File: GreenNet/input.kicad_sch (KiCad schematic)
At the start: 27 parts, among them U2 USB_C_Receptacle_12P, U3 USB_C_Receptacle_12P, U4 CP2102N-A02-GQFN28

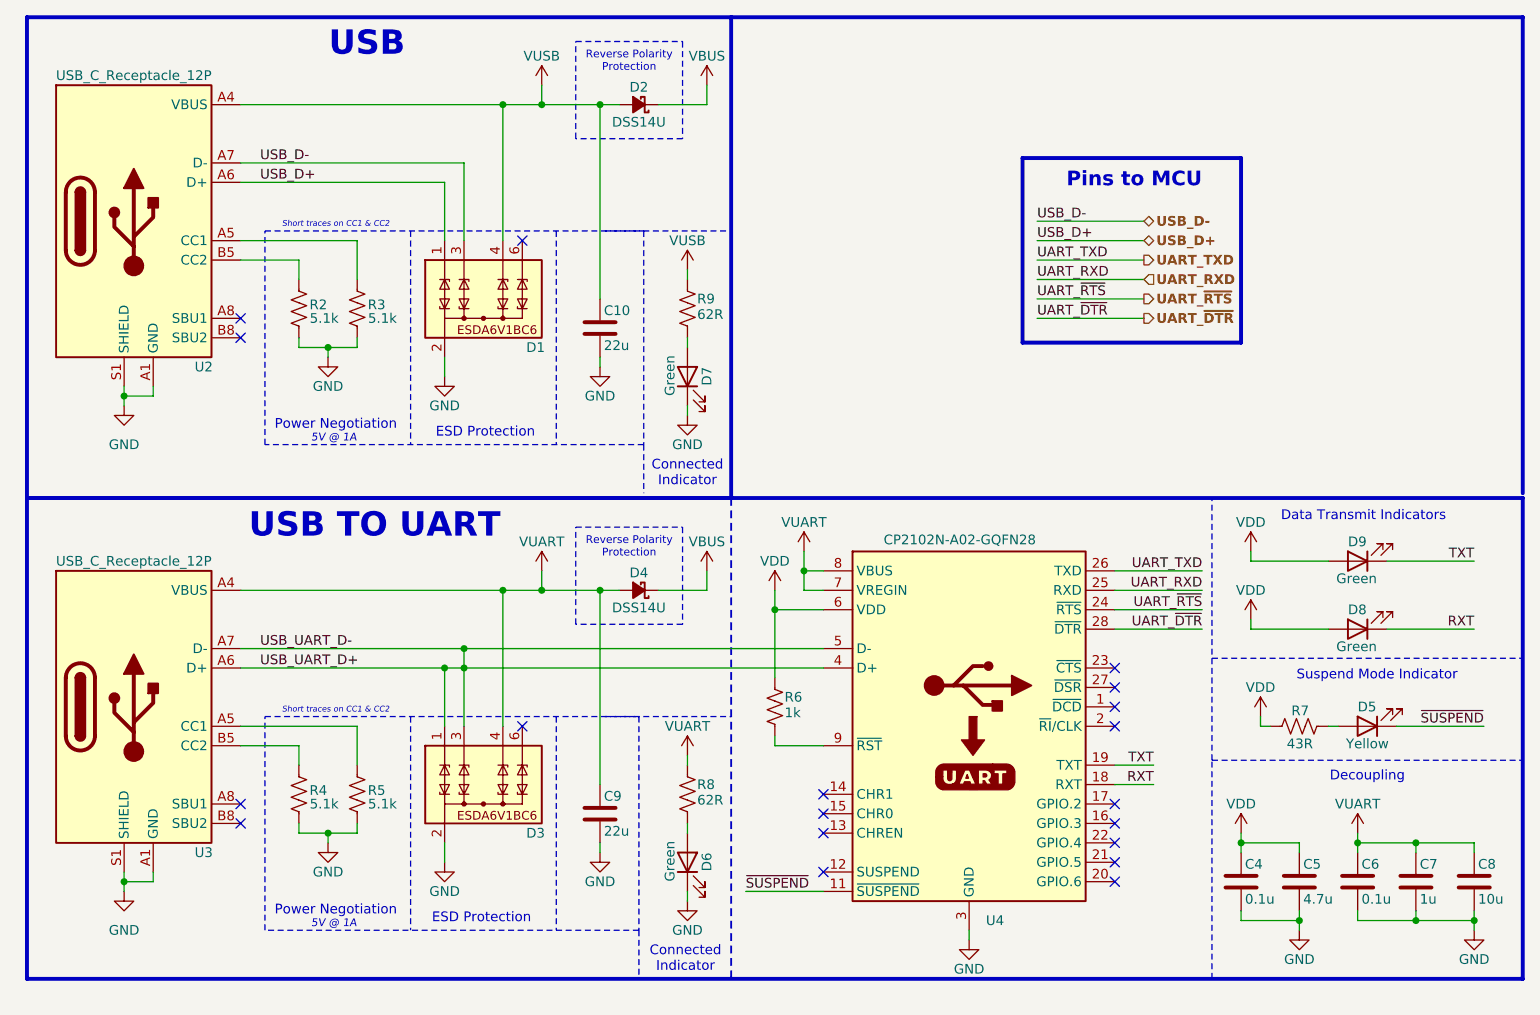
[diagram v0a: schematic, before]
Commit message: finished input schematic
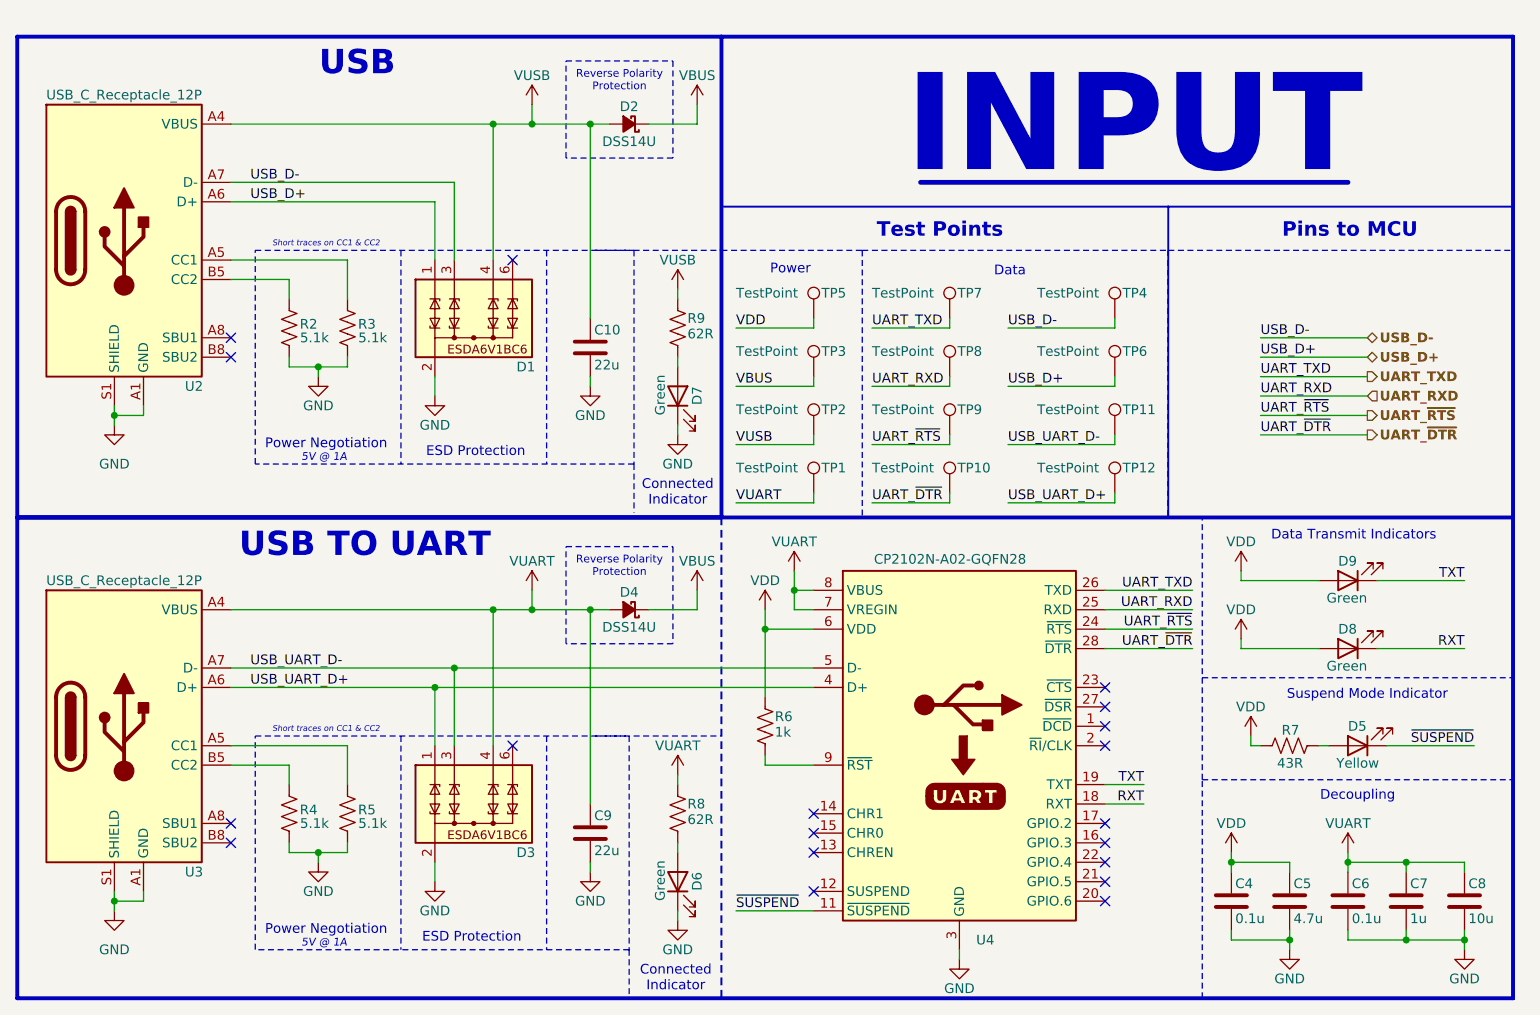
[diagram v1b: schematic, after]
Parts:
- added TP1, TP10, TP11, TP12, TP2, TP3, TP4, TP5, TP6, TP7, TP8, TP9: TestPoint, AA_TestPoints:RCWCTE, symbol Connector:TestPoint
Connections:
- net UART_RXD: now also TP8.1
- net UART_TXD: now also TP7.1
- net UART_~{DTR}: now also TP10.1
- net UART_~{RTS}: now also TP9.1
- net USB_D+: now also TP6.1
- net USB_D-: now also TP4.1
- net USB_UART_D+: now also TP12.1; no longer D3.3 (TVS2), U3.A7 (D-), U3.B7 (D-), U4.5 (D-)
- net VBUS: now also TP3.1
- net VDD: now also TP5.1
- net VUART: now also TP1.1
- net VUSB: now also TP2.1
- new net USB_UART_D-: D3.3 (TVS2), TP11.1, U3.A7 (D-), U3.B7 (D-), U4.5 (D-)
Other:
- note added: "Data"
- note added: "INPUT"
- note added: "Power"
- note added: "Test Points"
- moved on the sheet: C10, C4, C5, C6, C7, C8, C9, D1, D2, D3, D4, D5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

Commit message: USB-PC PD progress
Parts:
- removed R2, R3: 5.1k, Resistor_SMD:R_0805_2012Metric, symbol Device:R_US
- removed TP1, TP10, TP11, TP12, TP2, TP3, TP4, TP5, TP6, TP7, TP8, TP9: TestPoint, AA_TestPoints:RCWCTE, symbol Connector:TestPoint
- added Q4: IRF9358TRPBF, AA_FETS:SO8_IRF9358TRPBF_INF, symbol AA_FETs:IRF9358TRPBF
- added TP13, TP14, TP15, TP16, TP17, TP18, TP19, TP20, TP21, TP22, TP23, TP24: TestPoint, AA_TestPoints:RCWCTE, symbol Connector:TestPoint
- added U6: CYPD3177-24LQXQT, AA_Interface_USB:QFN50P400X400X60-25N-D, symbol AA_Interface_USB:CYPD3177-24LQXQT
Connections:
- net UART_RXD: now also TP18.1
- net UART_TXD: now also TP17.1
- net UART_~{DTR}: now also TP20.1
- net UART_~{RTS}: now also TP19.1
- net USB_D+: now also TP22.1
- net USB_D-: now also TP21.1
- net USB_UART_D+: now also TP24.1
- net USB_UART_D-: now also TP23.1
- net VBUS: now also TP14.1
- net VDD: no longer R6.1, U4.6 (VDD)
- net VUART: now also TP16.1
- net VUSB: now also TP15.1, U6.18 (VBUS_IN)
- net USB_CC1: now reaches U2.A5 (CC1)
- net USB_CC1: now also U6.15 (CC1)
- net USB_CC2: now reaches U2.B5 (CC2)
- net USB_CC2: now also U6.14 (CC2)
- net GND renamed EP
- net EP: now also U6.19 (GND), U6.22 (GND), U6.25 (EP)
- new net: U6.20 (DNU), U6.21 (DNU)
- new net: Q4.1 (S2), Q4.3 (S1)
- new net: Q4.5 (D1), Q4.6 (D1)
- new net ISINK_FINE: U6.6 (ISNK_FINE)
- new net ISNK_COARSE: U6.5 (ISNK_COARSE)
- new net SAFE_PWR_EN: U6.4 (SAFE_PWR_EN)
- new net UART_VDD: R6.1, TP13.1, U4.6 (VDD)
- new net USB_FAULT: U6.9 (FAULT)
- new net USB_FLIP: U6.10 (FLIP)
- new net USB_GPIO: U6.8 (GPIO)
- new net USB_HPI_INT: U6.7 (HPI_INT)
- new net USB_HPI_SCL: U6.13 (HPI_SCL)
- new net USB_HPI_SDA: U6.12 (HPI_SDA)
- new net USB_VCC: U6.24 (VCCD)
- new net USB_VDC_OUT: Q4.7 (D2), Q4.8 (D2), U6.11 (VDC_OUT)
- new net USB_VDD: U6.23 (VDDD)
- new net VBUS_FET_EN: U6.3 (VBUS_FET_EN)
- new net VBUS_MAX: U6.2 (VBUS_MAX)
- new net VBUS_MIN: U6.1 (VBUS_MIN)
- no-connect marks 19 -> 21
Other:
- note added: "UART"
- note removed: "USB TO UART"
- moved on the sheet: C10, C4, C5, C6, C7, C8, C9, D1, D2, D3, D4, D5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

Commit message: input schematic finished
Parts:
- removed D1, D3: ESDA6V1BC6, Package_TO_SOT_SMD:SOT-23-6, symbol Power_Protection:ESDA6V1BC6
- removed D2, D4: DSS14U, AA_Diodes:SOD-123FL, symbol Device:D_Schottky_Small_Filled
- removed D7: Green, LED_SMD:LED_0805_2012Metric, symbol Device:LED
- removed Q4: IRF9358TRPBF, AA_FETS:SO8_IRF9358TRPBF_INF, symbol AA_FETs:IRF9358TRPBF
- added C11, C12, C17, C18: 1u, Capacitor_SMD:C_0805_2012Metric, symbol Device:C
- added C13, C14: 0.1u, Capacitor_SMD:C_0805_2012Metric, symbol Device:C
- added C15, C16: 390p, Capacitor_SMD:C_0805_2012Metric, symbol Device:C
- added D1, D2: D5V0M1U2S9, symbol Device:D_TVS_Filled
- added D10, D3, D4: D_TVS_Filled, symbol Device:D_TVS_Filled
- added D11: Green, LED_SMD:LED_0805_2012Metric, symbol Device:LED
- added D12: Red, LED_SMD:LED_0805_2012Metric, symbol Device:LED
- added D7: 10V, AA_Diodes:NHZ10C,115, symbol Device:D_Zener_Filled
- added Q3: IRF9358TRPBF, AA_FETS:SO8_IRF9358TRPBF_INF, symbol AA_FETs:IRF9358TRPBF
- added Q4: SI3932DV-T1-GE3, AA_FETS:TSOP_0DV-T1-E3_VIS, symbol AA_FETs:SI3932DV-T1-GE3
- added Q5: SI3993CDV-T1-GE3, AA_FETS:TSOP_0DV-T1-E3_VIS, symbol AA_FETs:SI3993CDV-T1-GE3
- added R12, R14, R16: 49.9k, Resistor_SMD:R_0805_2012Metric, symbol Device:R_US
- added R13, R2, R23: 1k, Resistor_SMD:R_0805_2012Metric, symbol Device:R_US
- added R15, R18, R19, R20: 62R, Resistor_SMD:R_0805_2012Metric, symbol Device:R_US
- added R22, R24: 5.1k, Resistor_SMD:R_0805_2012Metric, symbol Device:R_US
- added R25: 2.4k, Resistor_SMD:R_0805_2012Metric, symbol Device:R_US
- added R3: 10k, Resistor_SMD:R_0805_2012Metric, symbol Device:R_US
- added TP1, TP10, TP11, TP12, TP2, TP3, TP4, TP5, TP6, TP7, TP8, TP9: TestPoint, AA_TestPoints:RCWCTE, symbol Connector:TestPoint
- R7: value 43R -> 62R
- R9: value 62R -> 1k
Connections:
- net ISINK_FINE is gone; now on net EP: U6.6 (ISNK_FINE)
- net USB_VDC_OUT is gone; now on net VBUS: U6.11 (VDC_OUT)
- net VBUS_MIN is gone; now on net EP: U6.1 (VBUS_MIN)
- net EP: now also C13.2, C14.2, C15.2, C16.2, C17.2, C18.2, D1.1 (A1), D10.1 (A1), D11.1 (K), D12.1 (K), D2.1 (A1), D3.1 (A1), D4.1 (A1), R16.1, R23.2, R25.2, TP3.1, TP5.1
- net ISNK_COARSE: now also R24.2, R25.1, TP6.1
- net SAFE_PWR_EN: now also R13.2, TP12.1
- net UART_VDD: now also C4.1, C5.1, R7.1, R18.1, R19.1, R2.2
- net USB_CC1: now also C15.1
- net USB_CC2: now also C16.1
- net USB_D+: now also D1.2 (A2)
- net USB_D-: now also D10.2 (A2)
- net USB_FAULT: now also R20.1
- net USB_UART_D+: now also D2.2 (A2)
- net USB_UART_D-: now also D3.2 (A2)
- net USB_VCC: now also C17.1, TP2.1
- net USB_VDD: now also C13.1, C14.1, C18.1, R15.1, R22.1, R24.1, TP1.1
- net VBUS: now also TP16.1, C12.2, Q3.5 (D1), Q3.6 (D1), Q4.6 (D1), Q5.6 (D1); no longer TP14.1
- net VBUS_FET_EN: now also R9.2, TP11.1
- net VBUS_MAX: now also R22.2, R23.1, TP4.1
- net VUART: now also TP14.1, D4.2 (A2), Q4.4 (D2); no longer TP16.1
- net VUSB: now also C11.2, Q3.7 (D2), Q3.8 (D2), Q5.4 (D2), R14.2, R3.2; no longer R9.1
- net USB_FLIP: no longer names the net of U6.10 (FLIP)
- net USB_GPIO renamed USB_PD_GPIO
- net USB_PD_GPIO: now also TP10.1
- net USB_HPI_INT renamed USB_PD_HPI_INT
- net USB_PD_HPI_INT: now also TP9.1
- net USB_HPI_SCL renamed USB_PD_HPI_SCL
- net USB_PD_HPI_SCL: now also TP8.1
- net USB_HPI_SDA renamed USB_PD_HPI_SDA
- net USB_PD_HPI_SDA: now also TP7.1
- removed net VDD: C4.1, C5.1, D8.2 (A), D9.2 (A), R7.1
- new net: D12.2 (A), R20.2
- new net: D9.2 (A), R18.2
- new net: D11.2 (A), R15.2
- new net: D8.2 (A), R19.2
- new net: Q4.1 (G1), Q4.3 (G2), R16.2, R2.1
- new net: Q4.2 (S2), Q4.5 (S1)
- new net: Q5.1 (G1), Q5.3 (G2), R13.1, R14.1
- new net: Q5.2 (S2), Q5.5 (S1)
- new net FET_GATE: C11.1, C12.1, D7.2 (A), Q3.2 (G2), Q3.4 (G1), R12.1, R3.1, R9.1
- new net FET_SRC: D7.1 (K), Q3.1 (S2), Q3.3 (S1), R12.2
- no-connect marks 21 -> 20
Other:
- note added: "0mA"
- note added: "2A"
- note added: "5V"
- note added: "9V"
- note added: "Backup Power FET"
- note added: "Limit V_{gs} to 10V"
- note added: "Main Power FET"
- note added: "Power FET"
- note added: "Power Request Fault Indicator"
- note added: "Power Request Settings"
- note removed: "Reverse Polarity Protection"
- moved on the sheet: C10, C4, C5, C6, C7, C8, C9, D5, D8, D9, R4, R5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

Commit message: started layout
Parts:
- D1, D2: footprint (none) -> AA_Diodes:D5V0M1U2S9Q; symbol Device:D_TVS_Filled -> Device:D_Zener_Filled
- D10, D3, D4: value D_TVS_Filled -> D5V0M1U2S9; footprint (none) -> AA_Diodes:D5V0M1U2S9Q; symbol Device:D_TVS_Filled -> Device:D_Zener_Filled
- D11, D12, D5, D6, D8, D9: symbol Device:LED -> Device:LED_Filled
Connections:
- net EP: now also D1.2 (A), D10.2 (A), D2.2 (A), D3.2 (A), D4.2 (A); no longer D1.1 (A1), D10.1 (A1), D2.1 (A1), D3.1 (A1), D4.1 (A1)
- net USB_D+: now also D1.1 (K); no longer D1.2 (A2)
- net USB_D-: now also D10.1 (K); no longer D10.2 (A2)
- net USB_UART_D+: now also D2.1 (K); no longer D2.2 (A2)
- net USB_UART_D-: now also D3.1 (K); no longer D3.2 (A2)
- net VUART: now also D4.1 (K); no longer D4.2 (A2)
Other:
- note added: "USB Power Delivery Controller"
- note added: "USB to UART"
- moved on the sheet: R6, U4

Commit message: more sensor work
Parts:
- removed TP3, TP5: TestPoint, AA_TestPoints:RCWCTE, symbol Connector:TestPoint
- C10, C9: value 22u -> 10u
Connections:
- net USB_PD_HPI_INT renamed USB_PD_INT
- net USB_PD_HPI_SCL renamed USB_PD_SCL
- net USB_PD_HPI_SDA renamed USB_PD_SDA
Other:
- moved on the sheet: TP10, TP4, TP6

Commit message: significant progress
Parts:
- removed TP7, TP8: TestPoint, AA_TestPoints:RCWCTE, symbol Connector:TestPoint
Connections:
- net UART_VDD: no longer R18.1, R19.1, R7.1
- net USB_PD_SCL renamed PWR_SCL
- net USB_PD_SDA renamed PWR_SDA
- new net +3.3V: R18.1, R19.1, R7.1
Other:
- note added: "PINS TO MCU"
- note added: "TEST POINTS"
- note removed: "Pins to MCU"
- note removed: "Test Points"
- moved on the sheet: TP6, TP9

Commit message: update
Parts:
- removed D10: D5V0M1U2S9, AA_Diodes:D5V0M1U2S9Q, symbol Device:D_Zener_Filled
- removed D11, D8, D9: Green, LED_SMD:LED_0805_2012Metric, symbol Device:LED_Filled
- removed D12: Red, LED_SMD:LED_0805_2012Metric, symbol Device:LED_Filled
- removed D5: Yellow, LED_SMD:LED_0805_2012Metric, symbol Device:LED_Filled
- removed D7: 10V, AA_Diodes:NHZ10C,115, symbol Device:D_Zener_Filled
- removed Q3: IRF9358TRPBF, AA_FETS:SO8_IRF9358TRPBF_INF, symbol AA_FETs:IRF9358TRPBF
- removed Q4: SI3932DV-T1-GE3, AA_FETS:TSOP_0DV-T1-E3_VIS, symbol AA_FETs:SI3932DV-T1-GE3
- removed Q5: SI3993CDV-T1-GE3, AA_FETS:TSOP_0DV-T1-E3_VIS, symbol AA_FETs:SI3993CDV-T1-GE3
- removed R12, R14, R16: 49.9k, Resistor_SMD:R_0805_2012Metric, symbol Device:R_US
- removed R13, R2, R23: 1k, Resistor_SMD:R_0805_2012Metric, symbol Device:R_US
- removed R15, R18, R19, R20, R7: 62R, Resistor_SMD:R_0805_2012Metric, symbol Device:R_US
- removed R22, R24: 5.1k, Resistor_SMD:R_0805_2012Metric, symbol Device:R_US
- removed R25: 2.4k, Resistor_SMD:R_0805_2012Metric, symbol Device:R_US
- removed R3: 10k, Resistor_SMD:R_0805_2012Metric, symbol Device:R_US
- removed TP1, TP10, TP11, TP12, TP2, TP4, TP6, TP9: TestPoint, AA_TestPoints:RCWCTE, symbol Connector:TestPoint
- removed U2: USB_C_Receptacle_12P, AA_Connectors:GCT_USB4105-GF-A, symbol AA_Connectors:USB_C_Receptacle_12P
- removed U6: CYPD3177-24LQXQT, AA_Interface_USB:QFN50P400X400X60-25N-D, symbol AA_Interface_USB:CYPD3177-24LQXQT
- added 3.9u: L, symbol Device:L
- added C20: 0.1u, Capacitor_SMD:C_0805_2012Metric, symbol Device:C
- added C21: 22u, Capacitor_SMD:C_0805_2012Metric, symbol Device:C
- added D10, D7: DSS14U, symbol Device:D_Schottky_Filled
- added D17, D18: D5V0M1U2S9, AA_Diodes:D5V0M1U2S9Q, symbol Device:D_Zener_Filled
- added D19: Green, LED_SMD:LED_0805_2012Metric, symbol Device:LED_Filled
- added J1: Conn_01x03_Pin, AA_Connectors:61300311121, symbol Connector:Conn_01x03_Pin
- added J4: Conn_01x04_Pin, AA_Connectors:61300411121, symbol Connector:Conn_01x04_Pin
- added Q2, Q3: 2N7002K, Package_TO_SOT_SMD:SOT-23, symbol Transistor_FET:2N7002K
- added R10: 5.1k, Resistor_SMD:R_0805_2012Metric, symbol Device:R_US
- added R11: 150R, Resistor_SMD:R_0805_2012Metric, symbol Device:R_US
- added TP25, TP26, TP27, TP28, TP7, TP8: TestPoint, AA_TestPoints:RCWCTE, symbol Connector:TestPoint
- added U2: AP63203WU, Package_TO_SOT_SMD:TSOT-23-6, symbol Regulator_Switching:AP63203WU
- added U5: BME280, Package_LGA:Bosch_LGA-8_2.5x2.5mm_P0.65mm_ClockwisePinNumbering, symbol Sensor:BME280
- added U6: USB_C_Receptacle_12P, AA_Connectors:GCT_USB4105-GF-A, symbol AA_Connectors:USB_C_Receptacle_12P
- added U7: LTR-303ALS-01, OptoDevice:Lite-On_LTR-303ALS-01, symbol Sensor_Optical:LTR-303ALS-01
- C10: value 10u -> 0.1u
- C11, C17: value 1u -> 10u
- C12: value 1u -> 0.1u
- C13: value 0.1u -> 1u
- C14: value 0.1u -> 10p
- C15, C16: value 390p -> 10p
- C18: value 1u -> 22u
- R8: value 62R -> 150R
- R9: value 1k -> 5.1k
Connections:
- net USB_VCC is gone; now on net VBUS: C17.1
- net +3.3V: now also C10.1, C12.1, C13.1, C18.1, 3.9u.2, C21.1, Q2.2 (S), Q3.2 (S), U2.1 (FB), U5.2 (CSB), U5.6 (VDDIO), U5.8 (VDD), U7.1 (VDD)
- net USB_D+: now also U6.A6 (D+), U6.B6 (D+)
- net USB_D-: now also D17.1 (K), U6.A7 (D-), U6.B7 (D-)
- net VBUS: now also D10.1 (K), D7.1 (K), U2.2 (EN), U2.3 (IN); no longer C12.2
- net VUART: now also D10.2 (A)
- net VUSB: now also C11.1, D18.1 (K), D7.2 (A), R11.1, U6.A4 (VBUS), U6.B4 (VBUS); no longer C10.1, C11.2
- net EP renamed GND
- net GND: now also C11.2, C12.2, R9.1, C21.2, D17.2 (A), D18.2 (A), D19.1 (K), J1.3 (Pin_3), J4.4 (Pin_4), R10.1, U2.4 (GND), U5.1 (GND), U5.5 (SDO), U5.7 (GND), U6.A1 (GND), U6.B1 (GND), U6.S1 (SHIELD), U7.3 (GND)
- removed net FET_GATE: C11.1, C12.1, R9.1
- net USB_CC1 renamed PERI_SCL
- net PERI_SCL: now also J4.1 (Pin_1), U5.4 (SCK), U7.4 (SCL)
- net USB_CC2 renamed LTR_INT
- net LTR_INT: now also TP7.1, U7.5 (INT)
- removed net USB_VDD: C13.1, C14.1, C18.1
- net VBUS_FET_EN: no longer names the net of R9.2
- net VBUS_FET_EN: now also U6.B5 (CC2)
- new net: 3.9u.1, C20.1, U2.5 (SW)
- new net: D19.2 (A), R11.2
- new net: C20.2, U2.6 (BST)
- new net: R10.2, U6.A5 (CC1)
- new net LCD_EN: Q3.1 (G), TP8.1
- new net LCD_PWR: J4.3 (Pin_3), Q3.3 (D), TP25.1
- new net PERI_SDA: C14.1, J4.2 (Pin_2), U5.3 (SDI), U7.6 (SDA)
- new net SOIL_EN: Q2.1 (G), TP27.1
- new net SOIL_PWR: J1.2 (Pin_2), Q2.3 (D), TP28.1
- new net SOIL_SENSE: J1.1 (Pin_1), TP26.1
- no-connect marks 20 -> 17
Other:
- note added: "Ambient Light Sensor"
- note added: "LCD Module"
- note added: "PERIPHERALS"
- note added: "POWER"
- note added: "Reverse Polarity Protection"
- note added: "Soil Moisture Sensor"
- note added: "Temperature, Pressure, and Humidity Sensor"
- note removed: "0mA"
- note removed: "2A"
- note removed: "5V"
- note removed: "9V"
- note removed: "Backup Power FET"
- note removed: "Data Transmit Indicators"
- note removed: "Limit V_{gs} to 10V"
- note removed: "Main Power FET"
- note removed: "Power FET"
- note removed: "Power Request Fault Indicator"
- note removed: "Power Request Settings"
- note removed: "Suspend Mode Indicator"
- note removed: "USB Power Delivery Controller"
- moved on the sheet: C4, C5, C6, C7, C8, D6, R8

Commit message: schematic FINAL
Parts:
- removed J4: Conn_01x04_Pin, AA_Connectors:61300411121, symbol Connector:Conn_01x04_Pin
- removed Q3: 2N7002K, Package_TO_SOT_SMD:SOT-23, symbol Transistor_FET:2N7002K
- L1: renamed from 3.9u; value L -> 3.9u
- TP13: value TestPoint -> UART_VDD
- TP14: value TestPoint -> VUART
- TP15: value TestPoint -> VUSB
- TP16: value TestPoint -> VBUS
- TP25: value TestPoint -> LCD_PWR
- TP26: value TestPoint -> SOIL_SENSE
- TP27: value TestPoint -> SOIL_EN
- TP28: value TestPoint -> SOIL_PWR
- TP7: value TestPoint -> LTR_INT
- TP8: value TestPoint -> LCD_EN
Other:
- note removed: "LCD Module"
- moved on the sheet: C10, C12, C13, C14, C15, C16, J1, Q2, TP25, TP26, TP27, TP28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
